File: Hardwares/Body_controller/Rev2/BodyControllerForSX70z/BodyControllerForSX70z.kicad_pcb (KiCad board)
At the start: 2 copper layers, 20.3 x 63 mm, 22 parts, among them J1 FPC-0.5LX-12PH20, J2 Conn_01x04_Pin, U1 PCF8574ATS

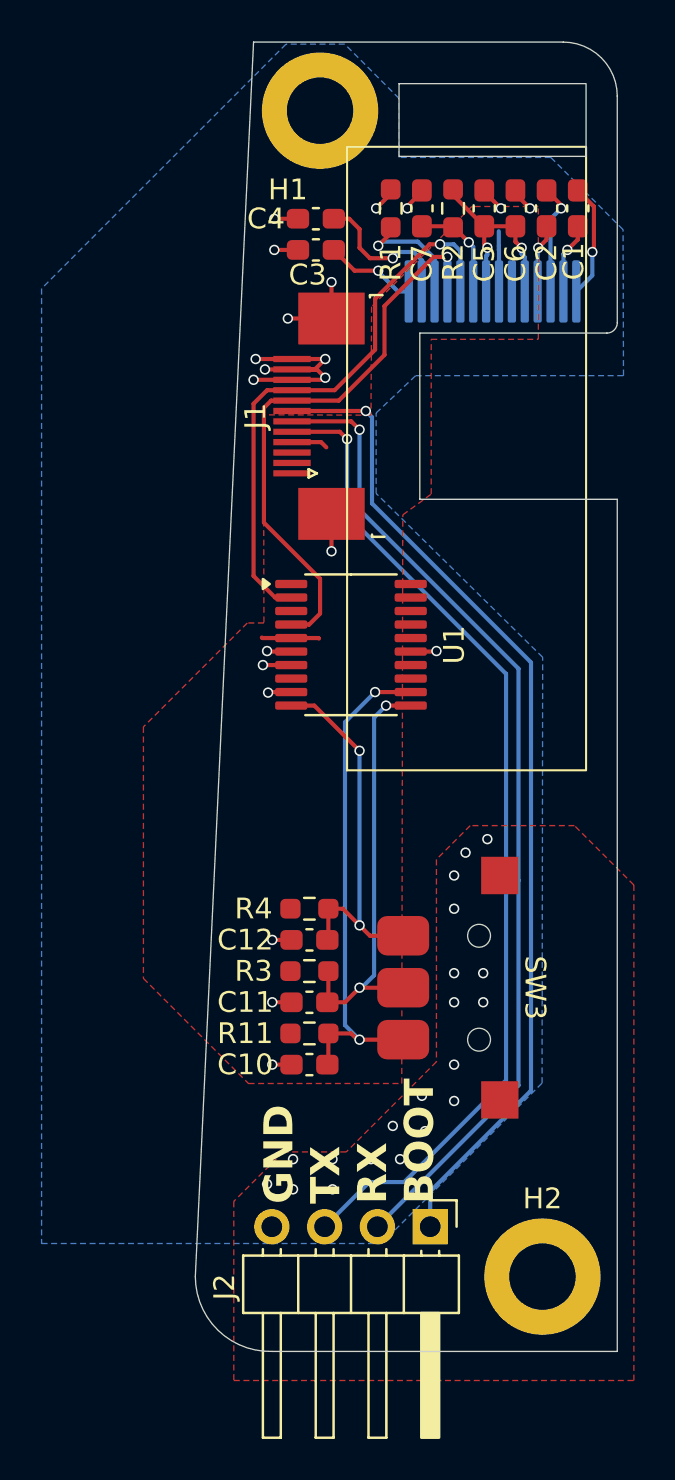
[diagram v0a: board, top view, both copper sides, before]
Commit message: BodyController Rev2: 机身控制器外壳设计 + PCB Layout 调整 + BOM
Co-Authored-By: Claude Sonnet 4.6 (1M context) <noreply@anthropic.com>
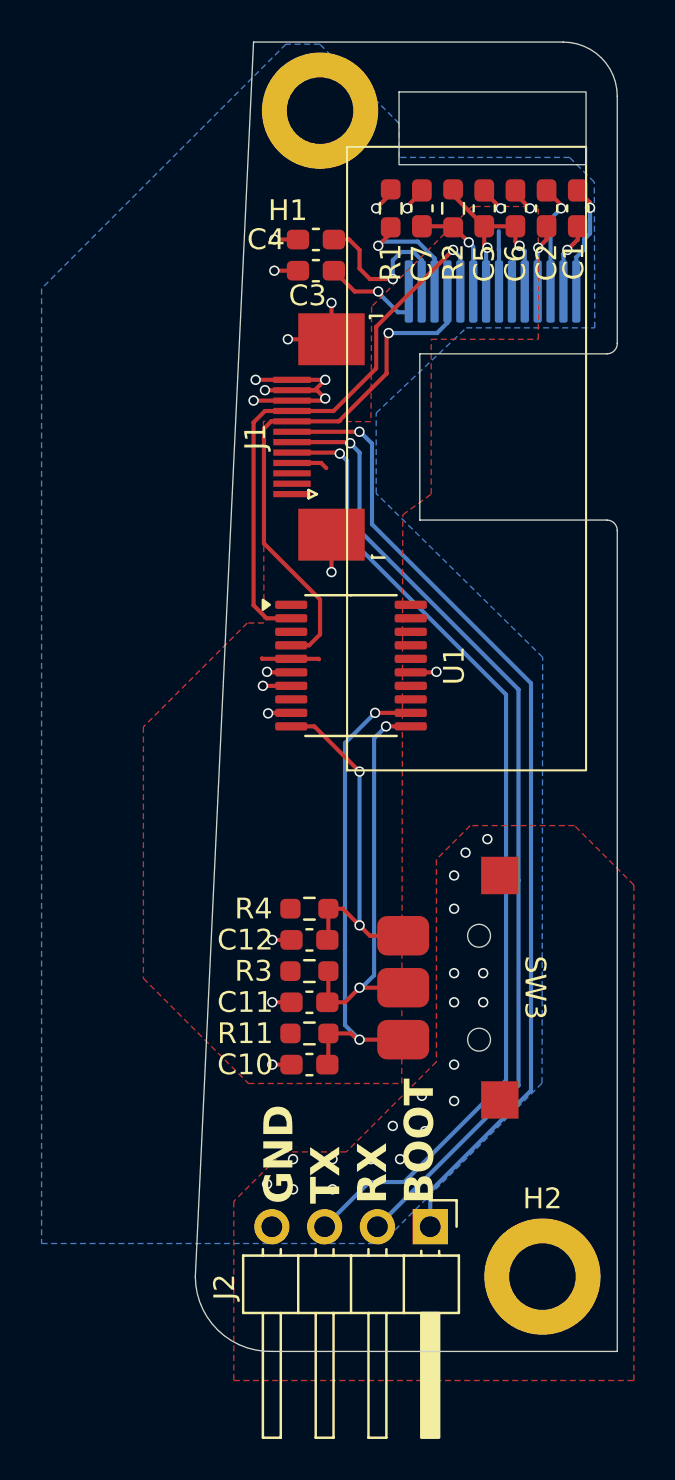
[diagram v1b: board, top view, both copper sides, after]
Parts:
- moved C3 1.00 mm to (105.8, 42.5)
- moved C4 1.00 mm to (105.8, 41.0)
- moved J1 1.00 mm to (106.0, 50.5)
- moved U1 1.00 mm to (107.5, 61.5)
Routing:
- net /SDA: track 27.5 -> 26.2 mm
- net /BOOT: track 48.1 -> 46.9 mm
- net /SW_PUSH: track 20.8 -> 19.7 mm
- net /SW_A: track 18.2 -> 17.2 mm
- net /SW_B: track 24.6 -> 23.5 mm
- net /RX: track 47.7 -> 46.7 mm
- net /TX: track 48.5 -> 47.4 mm
- net Net-(Disp1-C2N): track 3.42 -> 4.42 mm
- net Net-(Disp1-VCOM): track 7.34 -> 8.28 mm
- net Net-(Disp1-C2P): track 5.53 -> 6.38 mm
- net GND: track 35.0 -> 34.5 mm
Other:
- outline, holes or cut-outs redrawn
